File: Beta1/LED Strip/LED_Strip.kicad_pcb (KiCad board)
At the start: 2 copper layers, 163.2 x 8.9 mm, 100 parts, among them U0 APA102C, U1 APA102C, U10 APA102C, U11 APA102C, U12 APA102C, U13 APA102C, U14 APA102C, U15 APA102C, U2 APA102C, U3 APA102C, U4 APA102C, U5 APA102C, U6 APA102C, U7 APA102C, U8 APA102C, U9 APA102C

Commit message: Knob / LED Module WIP
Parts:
- added REF**: 1pin, Connect:1pin, F.Cu at (7.50, -12.6)
- added REF**: 1pin, Connect:1pin, F.Cu at (7.50, -3.00)
- added REF**: 1pin, Connect:1pin, F.Cu at (194.7, -12.6)
- added REF**: 1pin, Connect:1pin, F.Cu at (194.9, -3.00)
- moved C10 28.9 mm to (139.7, -9.72)
- moved C11 28.9 mm to (149.7, -9.72)
- moved C12 28.9 mm to (159.7, -9.72)
- moved C13 28.9 mm to (169.7, -9.72)
- moved C14 28.9 mm to (179.7, -9.72)
- moved C15 28.9 mm to (189.5, -10.3)
- moved C3 28.9 mm to (69.7, -9.72)
- moved C4 28.9 mm to (79.7, -9.72)
- moved C5 28.9 mm to (89.7, -9.72)
- moved C6 28.9 mm to (99.7, -9.72)
- moved C7 28.9 mm to (109.7, -9.72)
- moved C8 28.9 mm to (119.7, -9.72)
- moved C9 28.9 mm to (129.7, -9.72)
- moved CLK10 28.9 mm to (129.7, -11.7)
- moved CLK11 28.9 mm to (139.7, -11.7)
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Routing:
- net /CLK16: track 160.8 -> 2.95 mm, vias 1 -> 0
- net /D16: track 152.6 -> 1.54 mm
- net (no net): track 8.26 -> 0.00 mm
- net +5V: track 227.1 -> 222.1 mm
- net Net-(CLK0-Pad1): track 6.38 -> 1.54 mm
- net GND: track 179.6 -> 174.9 mm, vias 0 -> 1
- net Net-(D0-Pad1): track 3.61 -> 1.35 mm
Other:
- board size 163.2 x 8.9 mm -> 197.9 x 15.6 mm

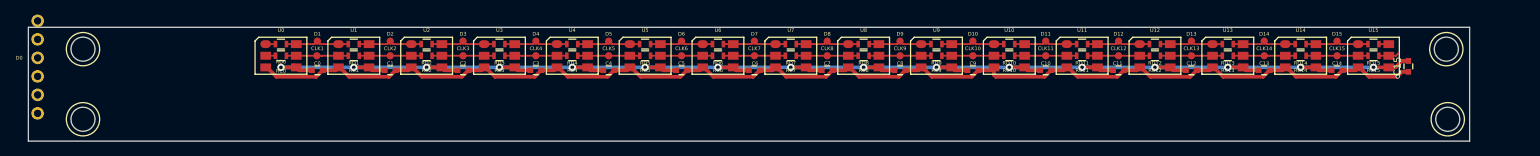
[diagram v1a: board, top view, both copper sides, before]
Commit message: Placed all LED components
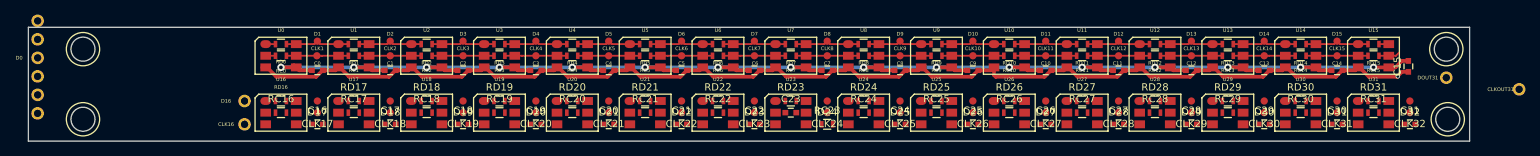
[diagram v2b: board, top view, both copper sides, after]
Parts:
- added C16: 0.1u, Capacitors_SMD:C_0603, F.Cu at (39.7, -2.31)
- added C17: 0.1u, Capacitors_SMD:C_0603, F.Cu at (49.7, -2.31)
- added C18: 0.1u, Capacitors_SMD:C_0603, F.Cu at (59.7, -2.31)
- added C19: 0.1u, Capacitors_SMD:C_0603, F.Cu at (69.7, -2.31)
- added C20: 0.1u, Capacitors_SMD:C_0603, F.Cu at (79.7, -2.31)
- added C21: 0.1u, Capacitors_SMD:C_0603, F.Cu at (89.7, -2.31)
- added C22: 0.1u, Capacitors_SMD:C_0603, F.Cu at (99.7, -2.31)
- added C23: 0.1u, Capacitors_SMD:C_0603, F.Cu at (104.7, -3.91)
- added C24: 0.1u, Capacitors_SMD:C_0603, F.Cu at (119.7, -2.31)
- added C25: 0.1u, Capacitors_SMD:C_0603, F.Cu at (129.7, -2.31)
- added C26: 0.1u, Capacitors_SMD:C_0603, F.Cu at (139.7, -2.31)
- added C27: 0.1u, Capacitors_SMD:C_0603, F.Cu at (149.7, -2.31)
- added C28: 0.1u, Capacitors_SMD:C_0603, F.Cu at (159.7, -2.31)
- added C29: 0.1u, Capacitors_SMD:C_0603, F.Cu at (169.7, -2.31)
- added C30: 0.1u, Capacitors_SMD:C_0603, F.Cu at (179.7, -2.31)
- added C31: 0.1u, Capacitors_SMD:C_0603, F.Cu at (189.7, -2.31)
- added CLK16: CONN_01X01, Liberry:single_0.1, F.Cu at (29.7, -2.31)
- added CLK17: CONN_01X01, Liberry:TESTPAD, F.Cu at (39.7, -3.91)
- added CLK18: CONN_01X01, Liberry:TESTPAD, F.Cu at (49.7, -3.91)
- added CLK19: CONN_01X01, Liberry:TESTPAD, F.Cu at (59.7, -3.91)
- added CLK20: CONN_01X01, Liberry:TESTPAD, F.Cu at (69.7, -3.91)
- added CLK21: CONN_01X01, Liberry:TESTPAD, F.Cu at (79.7, -3.91)
- added CLK22: CONN_01X01, Liberry:TESTPAD, F.Cu at (89.7, -3.91)
- added CLK23: CONN_01X01, Liberry:TESTPAD, F.Cu at (99.7, -3.91)
- added CLK24: CONN_01X01, Liberry:TESTPAD, F.Cu at (109.7, -3.91)
- added CLK25: CONN_01X01, Liberry:TESTPAD, F.Cu at (119.7, -3.91)
- added CLK26: CONN_01X01, Liberry:TESTPAD, F.Cu at (129.7, -3.91)
- added CLK27: CONN_01X01, Liberry:TESTPAD, F.Cu at (139.7, -3.91)
- added CLK28: CONN_01X01, Liberry:TESTPAD, F.Cu at (149.7, -3.91)
- added CLK29: CONN_01X01, Liberry:TESTPAD, F.Cu at (159.7, -3.91)
- added CLK30: CONN_01X01, Liberry:TESTPAD, F.Cu at (169.7, -3.91)
- added CLK31: CONN_01X01, Liberry:TESTPAD, F.Cu at (179.7, -3.91)
- added CLK32: CONN_01X01, Liberry:TESTPAD, F.Cu at (189.7, -3.91)
- added CLKOUT31: CONN_01X01, Liberry:single_0.1, F.Cu at (204.7, -7.11)
- added D16: CONN_01X01, Liberry:single_0.1, F.Cu at (29.7, -5.51)
- added D17: CONN_01X01, Liberry:TESTPAD, F.Cu at (39.7, -5.51)
- added D18: CONN_01X01, Liberry:TESTPAD, F.Cu at (49.7, -5.51)
- added D19: CONN_01X01, Liberry:TESTPAD, F.Cu at (59.7, -5.51)
- added D20: CONN_01X01, Liberry:TESTPAD, F.Cu at (69.7, -5.51)
- added D21: CONN_01X01, Liberry:TESTPAD, F.Cu at (79.7, -5.51)
- added D22: CONN_01X01, Liberry:TESTPAD, F.Cu at (89.7, -5.51)
- added D23: CONN_01X01, Liberry:TESTPAD, F.Cu at (99.7, -5.51)
- added D24: CONN_01X01, Liberry:TESTPAD, F.Cu at (109.7, -5.51)
- added D25: CONN_01X01, Liberry:TESTPAD, F.Cu at (119.7, -5.51)
- added D26: CONN_01X01, Liberry:TESTPAD, F.Cu at (129.7, -5.51)
- added D27: CONN_01X01, Liberry:TESTPAD, F.Cu at (139.7, -5.51)
- added D28: CONN_01X01, Liberry:TESTPAD, F.Cu at (149.7, -5.51)
- added D29: CONN_01X01, Liberry:TESTPAD, F.Cu at (159.7, -5.51)
- added D30: CONN_01X01, Liberry:TESTPAD, F.Cu at (169.7, -5.51)
- added D31: CONN_01X01, Liberry:TESTPAD, F.Cu at (179.7, -5.51)
- added D32: CONN_01X01, Liberry:TESTPAD, F.Cu at (189.7, -5.51)
- added DOUT31: CONN_01X01, Liberry:single_0.1, F.Cu at (194.7, -8.71)
- added RC16: ZERO, Resistors_SMD:R_0603, F.Cu at (34.7, -3.91)
- added RC17: ZERO, Resistors_SMD:R_0603, F.Cu at (44.7, -3.91)
- added RC18: ZERO, Resistors_SMD:R_0603, F.Cu at (54.7, -3.91)
- added RC19: ZERO, Resistors_SMD:R_0603, F.Cu at (64.7, -3.91)
- added RC20: ZERO, Resistors_SMD:R_0603, F.Cu at (74.7, -3.91)
- added RC21: ZERO, Resistors_SMD:R_0603, F.Cu at (84.7, -3.91)
- added RC22: ZERO, Resistors_SMD:R_0603, F.Cu at (94.7, -3.91)
- added RC23: ZERO, Resistors_SMD:R_0603, F.Cu at (109.7, -2.31)
- added RC24: ZERO, Resistors_SMD:R_0603, F.Cu at (114.7, -3.91)
- added RC25: ZERO, Resistors_SMD:R_0603, F.Cu at (124.7, -3.91)
- added RC26: ZERO, Resistors_SMD:R_0603, F.Cu at (134.7, -3.91)
- added RC27: ZERO, Resistors_SMD:R_0603, F.Cu at (144.7, -3.91)
- added RC28: ZERO, Resistors_SMD:R_0603, F.Cu at (154.7, -3.91)
- added RC29: ZERO, Resistors_SMD:R_0603, F.Cu at (164.7, -3.91)
- added RC30: ZERO, Resistors_SMD:R_0603, F.Cu at (174.7, -3.91)
- added RC31: ZERO, Resistors_SMD:R_0603, F.Cu at (184.7, -3.91)
- added RD16: ZERO, Resistors_SMD:R_0603, F.Cu at (34.7, -5.51)
- added RD17: ZERO, Resistors_SMD:R_0603, F.Cu at (44.7, -5.51)
- added RD18: ZERO, Resistors_SMD:R_0603, F.Cu at (54.7, -5.51)
- added RD19: ZERO, Resistors_SMD:R_0603, F.Cu at (64.7, -5.51)
- added RD20: ZERO, Resistors_SMD:R_0603, F.Cu at (74.7, -5.51)
- added RD21: ZERO, Resistors_SMD:R_0603, F.Cu at (84.7, -5.51)
- added RD22: ZERO, Resistors_SMD:R_0603, F.Cu at (94.7, -5.51)
- added RD23: ZERO, Resistors_SMD:R_0603, F.Cu at (104.7, -5.51)
- added RD24: ZERO, Resistors_SMD:R_0603, F.Cu at (114.7, -5.51)
- added RD25: ZERO, Resistors_SMD:R_0603, F.Cu at (124.7, -5.51)
- added RD26: ZERO, Resistors_SMD:R_0603, F.Cu at (134.7, -5.51)
- added RD27: ZERO, Resistors_SMD:R_0603, F.Cu at (144.7, -5.51)
- added RD28: ZERO, Resistors_SMD:R_0603, F.Cu at (154.7, -5.51)
- added RD29: ZERO, Resistors_SMD:R_0603, F.Cu at (164.7, -5.51)
- added RD30: ZERO, Resistors_SMD:R_0603, F.Cu at (174.7, -5.51)
- added RD31: ZERO, Resistors_SMD:R_0603, F.Cu at (184.7, -5.51)
- added U16: APA102C, Liberry:PLCC6-1.6x4.2_LED, F.Cu at (34.7, -3.91)
- added U17: APA102C, Liberry:PLCC6-1.6x4.2_LED, F.Cu at (44.7, -3.91)
- added U18: APA102C, Liberry:PLCC6-1.6x4.2_LED, F.Cu at (54.7, -3.91)
- added U19: APA102C, Liberry:PLCC6-1.6x4.2_LED, F.Cu at (64.7, -3.91)
- added U20: APA102C, Liberry:PLCC6-1.6x4.2_LED, F.Cu at (74.7, -3.91)
- added U21: APA102C, Liberry:PLCC6-1.6x4.2_LED, F.Cu at (84.7, -3.91)
- added U22: APA102C, Liberry:PLCC6-1.6x4.2_LED, F.Cu at (94.7, -3.91)
- added U23: APA102C, Liberry:PLCC6-1.6x4.2_LED, F.Cu at (104.7, -3.91)
- added U24: APA102C, Liberry:PLCC6-1.6x4.2_LED, F.Cu at (114.7, -3.91)
- added U25: APA102C, Liberry:PLCC6-1.6x4.2_LED, F.Cu at (124.7, -3.91)
- added U26: APA102C, Liberry:PLCC6-1.6x4.2_LED, F.Cu at (134.7, -3.91)
- added U27: APA102C, Liberry:PLCC6-1.6x4.2_LED, F.Cu at (144.7, -3.91)
- added U28: APA102C, Liberry:PLCC6-1.6x4.2_LED, F.Cu at (154.7, -3.91)
- added U29: APA102C, Liberry:PLCC6-1.6x4.2_LED, F.Cu at (164.7, -3.91)
- added U30: APA102C, Liberry:PLCC6-1.6x4.2_LED, F.Cu at (174.7, -3.91)
- added U31: APA102C, Liberry:PLCC6-1.6x4.2_LED, F.Cu at (184.7, -3.91)

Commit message: Placed all LED strip components. Only routing remains
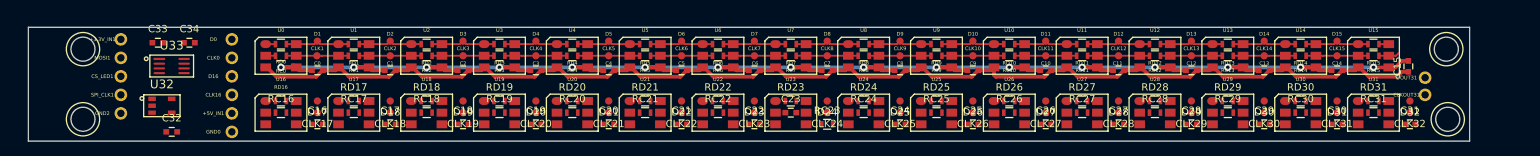
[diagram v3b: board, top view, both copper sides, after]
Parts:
- removed CLKOUT1, DOUT1, VCC0: CONN_01X01, Liberry:single_0.1
- added +3.3V_IN1: CONN_01X01, Liberry:single_0.1, F.Cu at (12.7, -14.0)
- added +5V_IN1: CONN_01X01, Liberry:single_0.1, F.Cu at (27.9, -3.81)
- added C32: 0.1u, Capacitors_SMD:C_0603, F.Cu at (19.7, -1.27)
- added C33: 0.1u, Capacitors_SMD:C_0603, F.Cu at (17.8, -13.5)
- added C34: 0.1u, Capacitors_SMD:C_0603, F.Cu at (22.1, -13.5)
- added CS_LED1: CONN_01X01, Liberry:single_0.1, F.Cu at (12.7, -8.89)
- added GND2: CONN_01X01, Liberry:single_0.1, F.Cu at (12.7, -3.81)
- added MOSI1: CONN_01X01, Liberry:single_0.1, F.Cu at (12.7, -11.4)
- added SPI_CLK1: CONN_01X01, Liberry:single_0.1, F.Cu at (12.7, -6.35)
- added U32: SN74LV1T125DBVR, Liberry:SOT23-5, F.Cu at (18.3, -4.86)
- added U33: SN74LVC2T45DCTT, Liberry:SSOP8, F.Cu at (19.7, -10.3)
- moved GND0 27.1 mm to (27.9, -1.27)
- moved CLK0 26.8 mm to (27.9, -11.4)
- moved D0 26.8 mm to (27.9, -14.0)
- moved CLKOUT31 12.9 mm to (191.8, -6.35)
- moved CLK16 4.40 mm to (27.9, -6.35)
- moved D16 3.80 mm to (27.9, -8.89)
- moved DOUT31 2.91 mm to (191.8, -8.71)

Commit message: Cleaned up reference designators on PCB
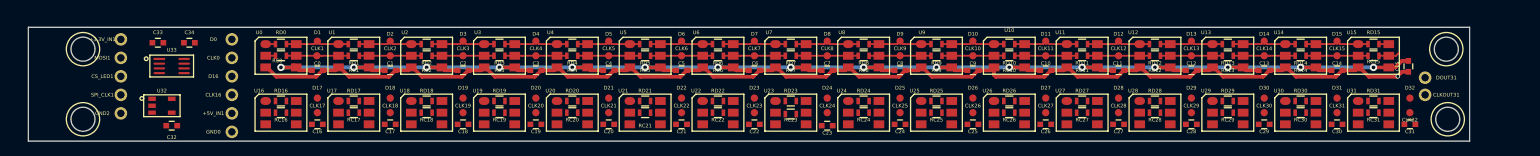
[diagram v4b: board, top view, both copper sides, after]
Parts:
- moved C23 5.31 mm to (109.7, -2.12)
- moved RC23 5.20 mm to (104.7, -3.72)
- moved C32 0.85 mm to (19.7, -2.12)
- moved D17 0.40 mm to (39.7, -5.91)
- moved D18 0.40 mm to (49.7, -5.91)
- moved D19 0.40 mm to (59.7, -5.91)
- moved D20 0.40 mm to (69.7, -5.91)
- moved D21 0.40 mm to (79.7, -5.91)
- moved D22 0.40 mm to (89.7, -5.91)
- moved D23 0.40 mm to (99.7, -5.91)
- moved D24 0.40 mm to (109.7, -5.91)
- moved D25 0.40 mm to (119.7, -5.91)
- moved D26 0.40 mm to (129.7, -5.91)
- moved D27 0.40 mm to (139.7, -5.91)
- moved D28 0.40 mm to (149.7, -5.91)
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
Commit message: Routed LED PCB; everything but 1 unconnected (or openGL render problem)
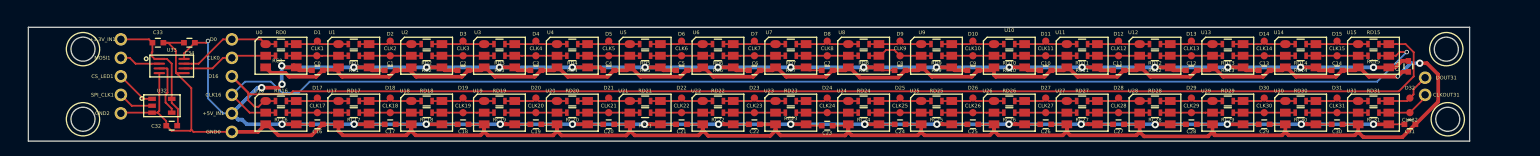
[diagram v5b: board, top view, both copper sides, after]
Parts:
- moved RC23 0.19 mm to (104.7, -3.91)
- turned C32 to 180 degrees
- turned C34 to 180 degrees
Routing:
- net GND: track 174.9 -> 456.3 mm, vias 1 -> 2
- net +5V: track 222.1 -> 477.2 mm, vias 16 -> 35
- net /D16: track 1.54 -> 181.7 mm
- net /CLK16: track 2.95 -> 176.0 mm, vias 0 -> 1
- net +3V3: track 0.00 -> 18.5 mm
- net Net-(D0-Pad1): track 1.35 -> 14.2 mm
- net Net-(CLK0-Pad1): track 1.54 -> 13.5 mm
- net /D24: track 0.00 -> 8.83 mm
- net Net-(D25-Pad1): track 0.00 -> 8.83 mm
- net Net-(D23-Pad1): track 0.00 -> 8.83 mm
- net Net-(D22-Pad1): track 0.00 -> 8.83 mm
- net Net-(D21-Pad1): track 0.00 -> 8.83 mm
- net Net-(D20-Pad1): track 0.00 -> 8.83 mm
- net Net-(D19-Pad1): track 0.00 -> 8.83 mm
- net Net-(D18-Pad1): track 0.00 -> 8.83 mm
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
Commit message: Trimmed outside edges from 7.5 to hole to 3mm to hole. Courage.
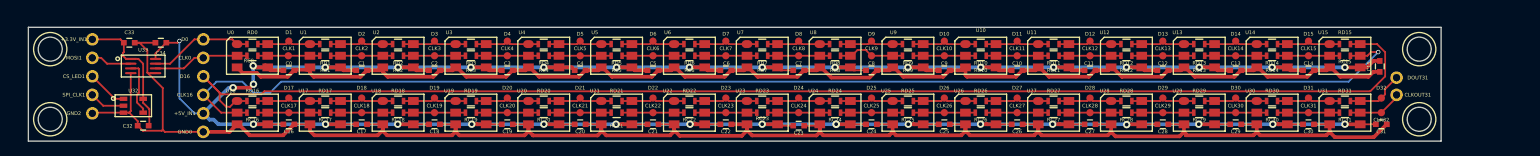
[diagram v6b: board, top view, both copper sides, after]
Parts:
- moved REF** 4.50 mm to (3.00, -12.6)
- moved REF** 4.50 mm to (3.00, -3.00)
- moved C10 3.92 mm to (135.8, -9.72)
- moved C11 3.92 mm to (145.8, -9.72)
- moved C12 3.92 mm to (155.8, -9.72)
- moved C13 3.92 mm to (165.8, -9.72)
- moved C14 3.92 mm to (175.8, -9.72)
- moved C26 3.92 mm to (135.8, -2.31)
- moved C27 3.92 mm to (145.8, -2.31)
- moved C28 3.92 mm to (155.8, -2.31)
- moved C29 3.92 mm to (165.8, -2.31)
- moved C30 3.92 mm to (175.8, -2.31)
- moved C31 3.92 mm to (185.8, -2.31)
- moved CLK11 3.92 mm to (135.8, -11.7)
- moved CLK12 3.92 mm to (145.8, -11.7)
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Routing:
- net GND: track 456.3 -> 441.2 mm, vias 2 -> 0
- net +5V: track 477.2 -> 476.3 mm
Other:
- board size 197.9 x 15.6 mm -> 194 x 15.6 mm

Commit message: Fixed a math error and adjusted height of led board + component heights
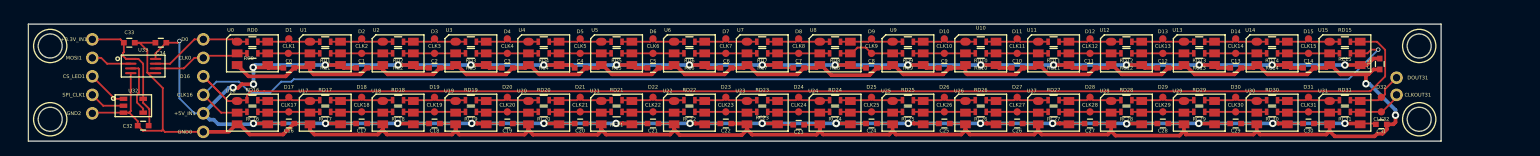
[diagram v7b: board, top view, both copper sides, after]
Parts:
- moved REF** 0.44 mm to (3.00, -13.1)
- moved REF** 0.44 mm to (191.0, -13.1)
- moved C0 0.33 mm to (35.8, -10.0)
- moved C1 0.33 mm to (45.8, -10.0)
- moved C10 0.33 mm to (135.8, -10.0)
- moved C11 0.33 mm to (145.8, -10.0)
- moved C12 0.33 mm to (155.8, -10.0)
- moved C13 0.33 mm to (165.8, -10.0)
- moved C14 0.33 mm to (175.8, -10.0)
- moved C15 0.33 mm to (185.6, -10.6)
- moved C2 0.33 mm to (55.8, -10.0)
- moved C3 0.33 mm to (65.8, -10.0)
- moved C4 0.33 mm to (75.8, -10.0)
- moved C5 0.33 mm to (85.8, -10.0)
- moved C6 0.33 mm to (95.8, -10.0)
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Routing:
- net GND: track 441.2 -> 450.9 mm, vias 0 -> 2
- net /D16: track 181.7 -> 177.9 mm
- net +5V: track 476.3 -> 475.4 mm
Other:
- board size 194 x 15.6 mm -> 194 x 16.1 mm

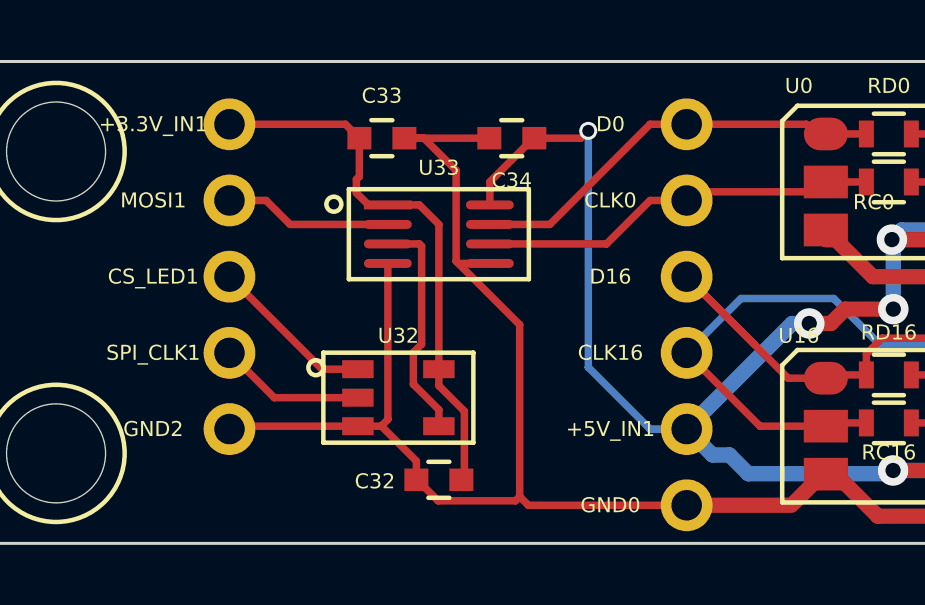
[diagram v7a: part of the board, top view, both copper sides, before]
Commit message: Added Duplicate row 0.1" header for novice daisy chaining / monitoring
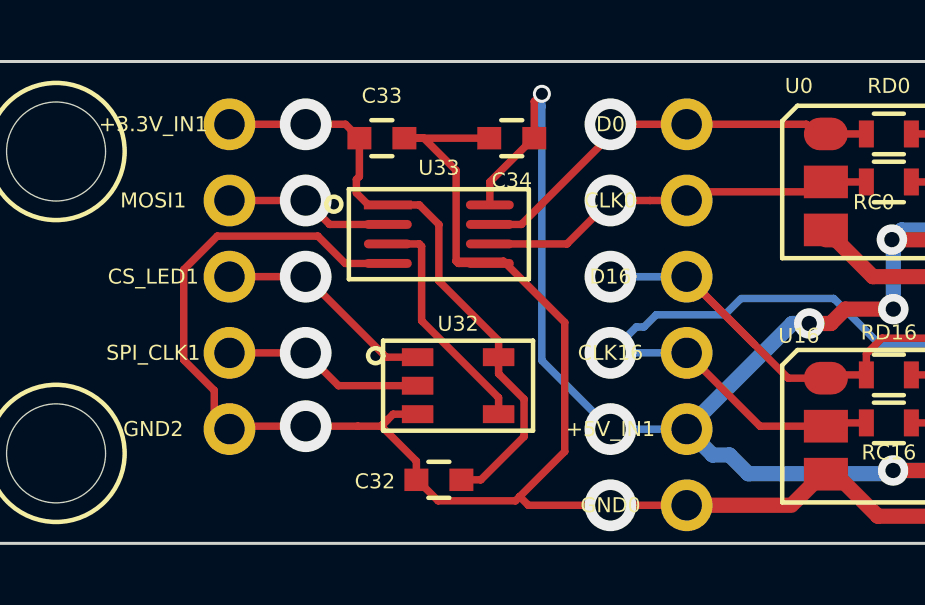
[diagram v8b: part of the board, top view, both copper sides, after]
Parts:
- moved U32 2.03 mm to (16.4, -5.26)
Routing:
- net GND: track 450.9 -> 462.9 mm, vias 2 -> 4
- net /CLK16: track 176.2 -> 181.2 mm, vias 1 -> 2
- net /D16: track 177.9 -> 180.4 mm, vias 0 -> 1
- net Net-(SPI_CLK1-Pad1): track 4.90 -> 7.25 mm, vias 0 -> 1
- net +5V: track 475.4 -> 477.8 mm, vias 35 -> 36
- net +3V3: track 18.5 -> 20.6 mm, vias 0 -> 1
- net Net-(CS_LED1-Pad1): track 5.56 -> 7.38 mm, vias 0 -> 1
- net Net-(D0-Pad1): track 14.2 -> 14.4 mm, vias 0 -> 1
- net Net-(CLK0-Pad1): vias 0 -> 1
- net Net-(MOSI1-Pad1): vias 0 -> 1
